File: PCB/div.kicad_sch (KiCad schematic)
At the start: 24 parts

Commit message: :wrench: Adjust project name on sheets
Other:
- title: The Count -> DIV
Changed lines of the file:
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@@
   (paper "A4")
   (title_block
-    (title "The Count")
+    (title "DIV")
     (date "2023-04-03")
     (rev "v1")

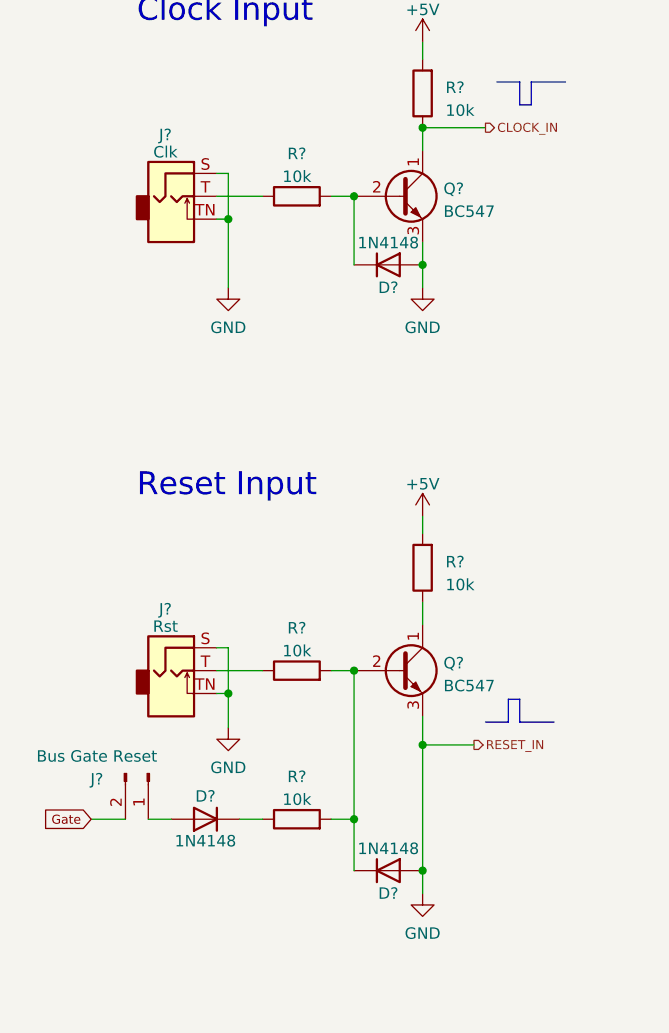
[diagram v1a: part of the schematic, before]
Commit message: :bug: Fix reset input circuit
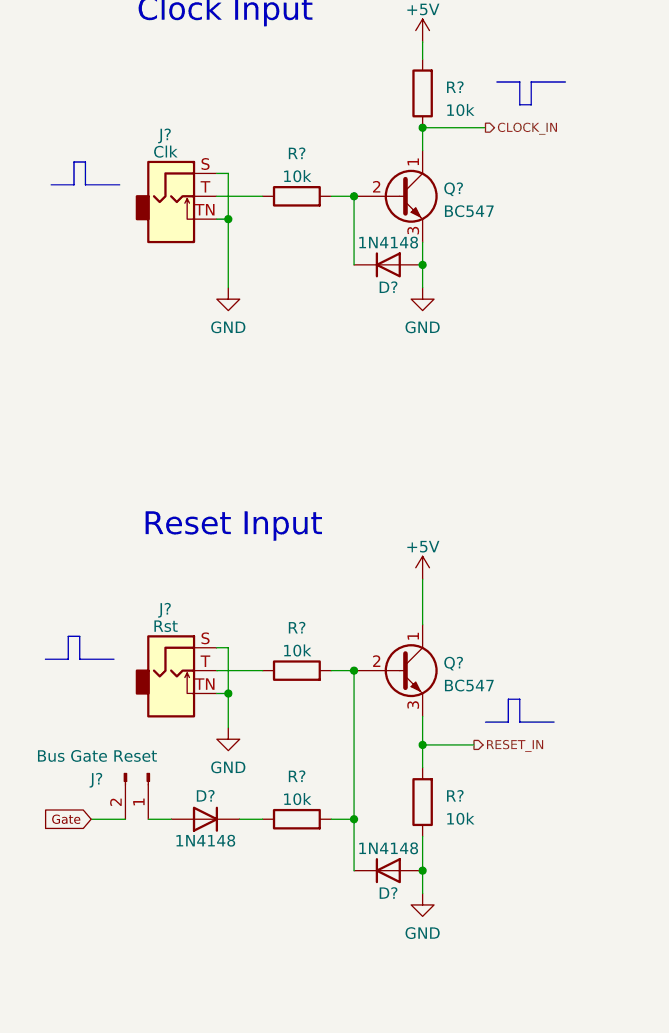
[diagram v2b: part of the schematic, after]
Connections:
- net +5V: now also Q?.1 (C); no longer R?.2
- net GND: now also R?.1; no longer D?.2 (A), Q?.3 (E), U?.2 (MR)
- new net RESET_IN: D?.2 (A), Q?.3 (E), R?.2, U?.2 (MR)
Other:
- moved on the sheet: R?
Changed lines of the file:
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@@
     (stroke (width 0) (type default))
+  )
+  (polyline (pts (xy 21.59 42.545) (xy 21.59 45.085))
+    (stroke (width 0) (type solid))
   )
   (polyline (pts (xy 68.58 104.775) (xy 68.58 102.235))
@@
     (stroke (width 0) (type default))
   )
+  (polyline (pts (xy 20.955 95.25) (xy 20.955 97.79))
+    (stroke (width 0) (type solid))
+  )
   (wire (pts (xy 169.545 74.93) (xy 169.545 78.74))
     (stroke (width 0) (type default))
@@
     (stroke (width 0) (type default))
   )
+  (polyline (pts (xy 19.685 95.25) (xy 20.955 95.25))
+    (stroke (width 0) (type solid))
+  )
   (wire (pts (xy 59.055 121.285) (xy 59.055 123.825))
     (stroke (width 0) (type default))
@@
     (stroke (width 0) (type default))
   )
-  (wire (pts (xy 59.055 81.915) (xy 59.055 83.82))
-    (stroke (width 0) (type default))
-  )
   (wire (pts (xy 36.195 101.6) (xy 37.465 101.6))
     (stroke (width 0) (type default))
@@
     (stroke (width 0) (type default))
   )
-  (wire (pts (xy 59.055 107.315) (xy 59.055 121.285))
+  (wire (pts (xy 59.055 107.315) (xy 59.055 109.855))
     (stroke (width 0) (type default))
   )
@@
     (stroke (width 0) (type default))
   )
+  (polyline (pts (xy 21.59 45.085) (xy 25.4 45.085))
+    (stroke (width 0) (type solid))
+  )
   (wire (pts (xy 46.99 184.15) (xy 46.99 186.69))
     (stroke (width 0) (type default))
@@
     (stroke (width 0) (type default))
   )
+  (polyline (pts (xy 20.32 45.085) (xy 20.32 42.545))
+    (stroke (width 0) (type solid))
+  )
+  (polyline (pts (xy 20.955 97.79) (xy 24.765 97.79))
+    (stroke (width 0) (type solid))
+  )
   (wire (pts (xy 91.44 184.15) (xy 109.22 184.15))
     (stroke (width 0) (type default))
@@
     (stroke (width 0) (type default))
   )
+  (polyline (pts (xy 17.78 45.085) (xy 20.32 45.085))
+    (stroke (width 0) (type solid))
+  )
   (wire (pts (xy 103.505 48.26) (xy 103.505 51.435))
     (stroke (width 0) (type default))
@@
     (stroke (width 0) (type default))
   )
+  (polyline (pts (xy 17.145 97.79) (xy 19.685 97.79))
+    (stroke (width 0) (type solid))
+  )
   (wire (pts (xy 201.93 98.425) (xy 223.52 98.425))
     (stroke (width 0) (type default))
   )
+  (polyline (pts (xy 20.32 42.545) (xy 21.59 42.545))
+    (stroke (width 0) (type solid))
+  )
   (wire (pts (xy 179.705 85.09) (xy 200.025 85.09))
     (stroke (width 0) (type default))
@@
     (stroke (width 0) (type default))
   )
+  (polyline (pts (xy 19.685 97.79) (xy 19.685 95.25))
+    (stroke (width 0) (type solid))
+  )
   (wire (pts (xy 109.22 173.99) (xy 109.22 176.53))
     (stroke (width 0) (type default))
@@
     (stroke (width 0) (type default))
   )
+  (wire (pts (xy 59.055 117.475) (xy 59.055 121.285))
+    (stroke (width 0) (type default))
+  )
   (wire (pts (xy 37.465 48.895) (xy 37.465 56.515))
     (stroke (width 0) (type default))
@@
     (stroke (width 0) (type default))
   )
-  (wire (pts (xy 59.055 91.44) (xy 59.055 93.98))
+  (wire (pts (xy 59.055 88.9) (xy 59.055 93.98))
     (stroke (width 0) (type default))
   )
@@
     (effects (font (size 1 1)) (justify right bottom))
   )
-  (text "Reset Input" (at 27.305 80.01 0)
+  (text "Reset Input" (at 27.94 84.455 0)
     (effects (font (size 2.54 2.54)) (justify left bottom))
   )
@@
     )
   )
-  (symbol (lib_id "Device:R") (at 59.055 87.63 180) (unit 1)
-    (in_bom yes) (on_board yes) (dnp no) (fields_autoplaced)
-    (property "Reference" "R?" (at 61.595 86.995 0)
+  (symbol (lib_id "Device:R") (at 59.055 113.665 180) (unit 1)
+    (in_bom yes) (on_board yes) (dnp no) (fields_autoplaced)
+    (property "Reference" "R?" (at 61.595 113.03 0)
       (effects (font (size 1.27 1.27)) (justify right))
     )
-    (property "Value" "10k" (at 61.595 89.535 0)
+    (property "Value" "10k" (at 61.595 115.57 0)
       (effects (font (size 1.27 1.27)) (justify right))
     )
-    (property "Footprint" "Resistor_THT:R_Axial_DIN0207_L6.3mm_D2.5mm_P7.62mm_Horizontal" (at 60.833 87.63 90)
-      (effects (font (size 1.27 1.27)) hide)
-    )
-    (property "Datasheet" "~" (at 59.055 87.63 0)
+    (property "Footprint" "Resistor_THT:R_Axial_DIN0207_L6.3mm_D2.5mm_P7.62mm_Horizontal" (at 60.833 113.665 90)
+      (effects (font (size 1.27 1.27)) hide)
+    )
+    (property "Datasheet" "~" (at 59.055 113.665 0)
       (effects (font (size 1.27 1.27)) hide)
     )
@@
     )
   )
-  (symbol (lib_id "power:+5V") (at 59.055 81.915 0) (unit 1)
-    (in_bom yes) (on_board yes) (dnp no) (fields_autoplaced)
-    (property "Reference" "#PWR?" (at 59.055 85.725 0)
-      (effects (font (size 1.27 1.27)) hide)
-    )
-    (property "Value" "+5V" (at 59.055 78.3392 0)
+  (symbol (lib_id "power:+5V") (at 59.055 88.9 0) (unit 1)
+    (in_bom yes) (on_board yes) (dnp no) (fields_autoplaced)
+    (property "Reference" "#PWR?" (at 59.055 92.71 0)
+      (effects (font (size 1.27 1.27)) hide)
+    )
+    (property "Value" "+5V" (at 59.055 85.3242 0)
       (effects (font (size 1.27 1.27)))
     )
-    (property "Footprint" "" (at 59.055 81.915 0)
-      (effects (font (size 1.27 1.27)) hide)
-    )
-    (property "Datasheet" "" (at 59.055 81.915 0)
-      (effects (font (size 1.27 1.27)) hide)
-    )
+    (property "Footprint" "" (at 59.055 88.9 0)
+      (effects (font (size 1.27 1.27)) hide)
+    )
+    (property "Datasheet" "" (at 59.055 88.9 0)
+      (effects (font (size 1.27 1.27)) hide)
+    )

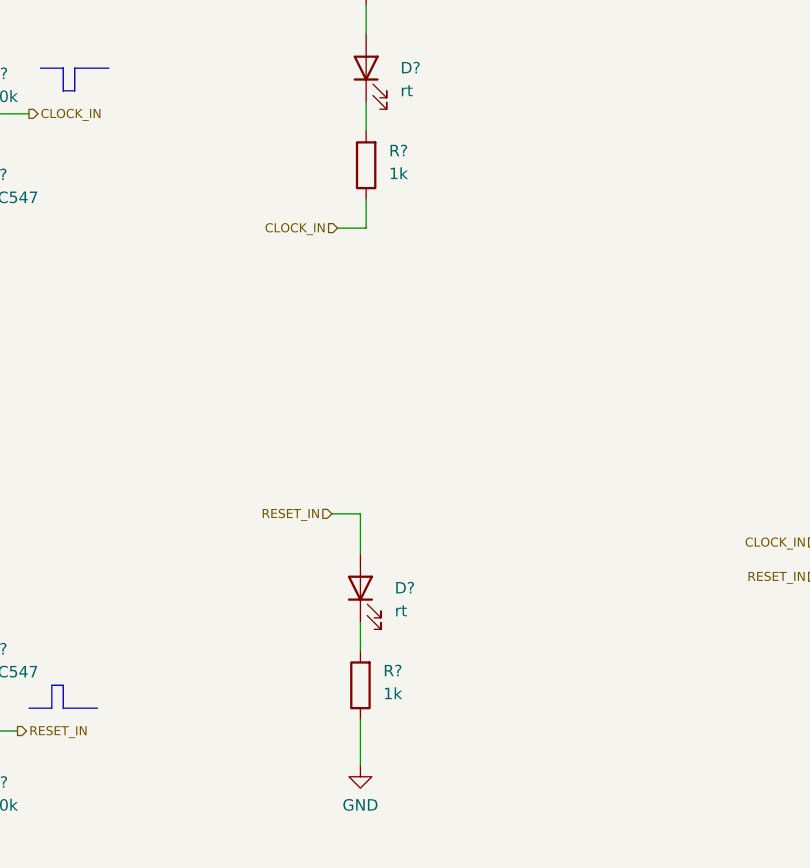
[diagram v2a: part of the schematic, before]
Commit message: :wrench: Adjust LED series resistors
With 4k7 the brightness is much better to look at.
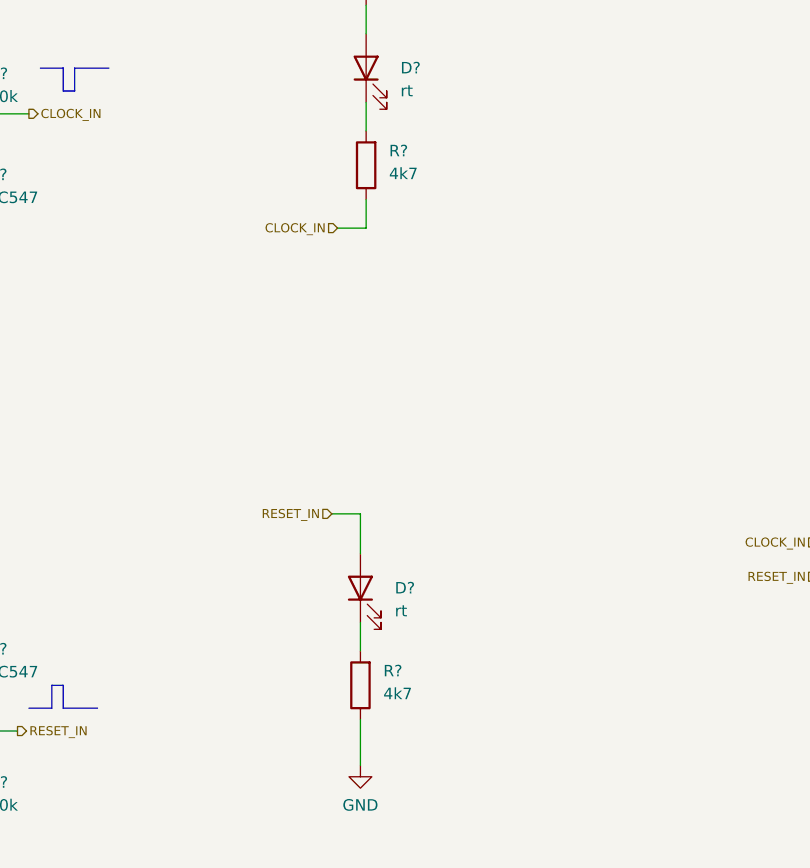
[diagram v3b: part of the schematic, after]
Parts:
- R? (x2): value 1k -> 4k7
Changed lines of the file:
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@@
       (effects (font (size 1.27 1.27)) (justify right))
     )
-    (property "Value" "1k" (at 106.045 45.4025 0)
+    (property "Value" "4k7" (at 106.045 45.4025 0)
       (effects (font (size 1.27 1.27)) (justify right))
     )
@@
       (effects (font (size 1.27 1.27)) (justify right))
     )
-    (property "Value" "1k" (at 105.41 103.1875 0)
-      (effects (font (size 1.27 1.27)) (justify right))
-    )
+    (property "Value" "4k7" (at 105.41 103.1875 0)
+      (effects (font (size 1.27 1.27)) (justify right))
+    )

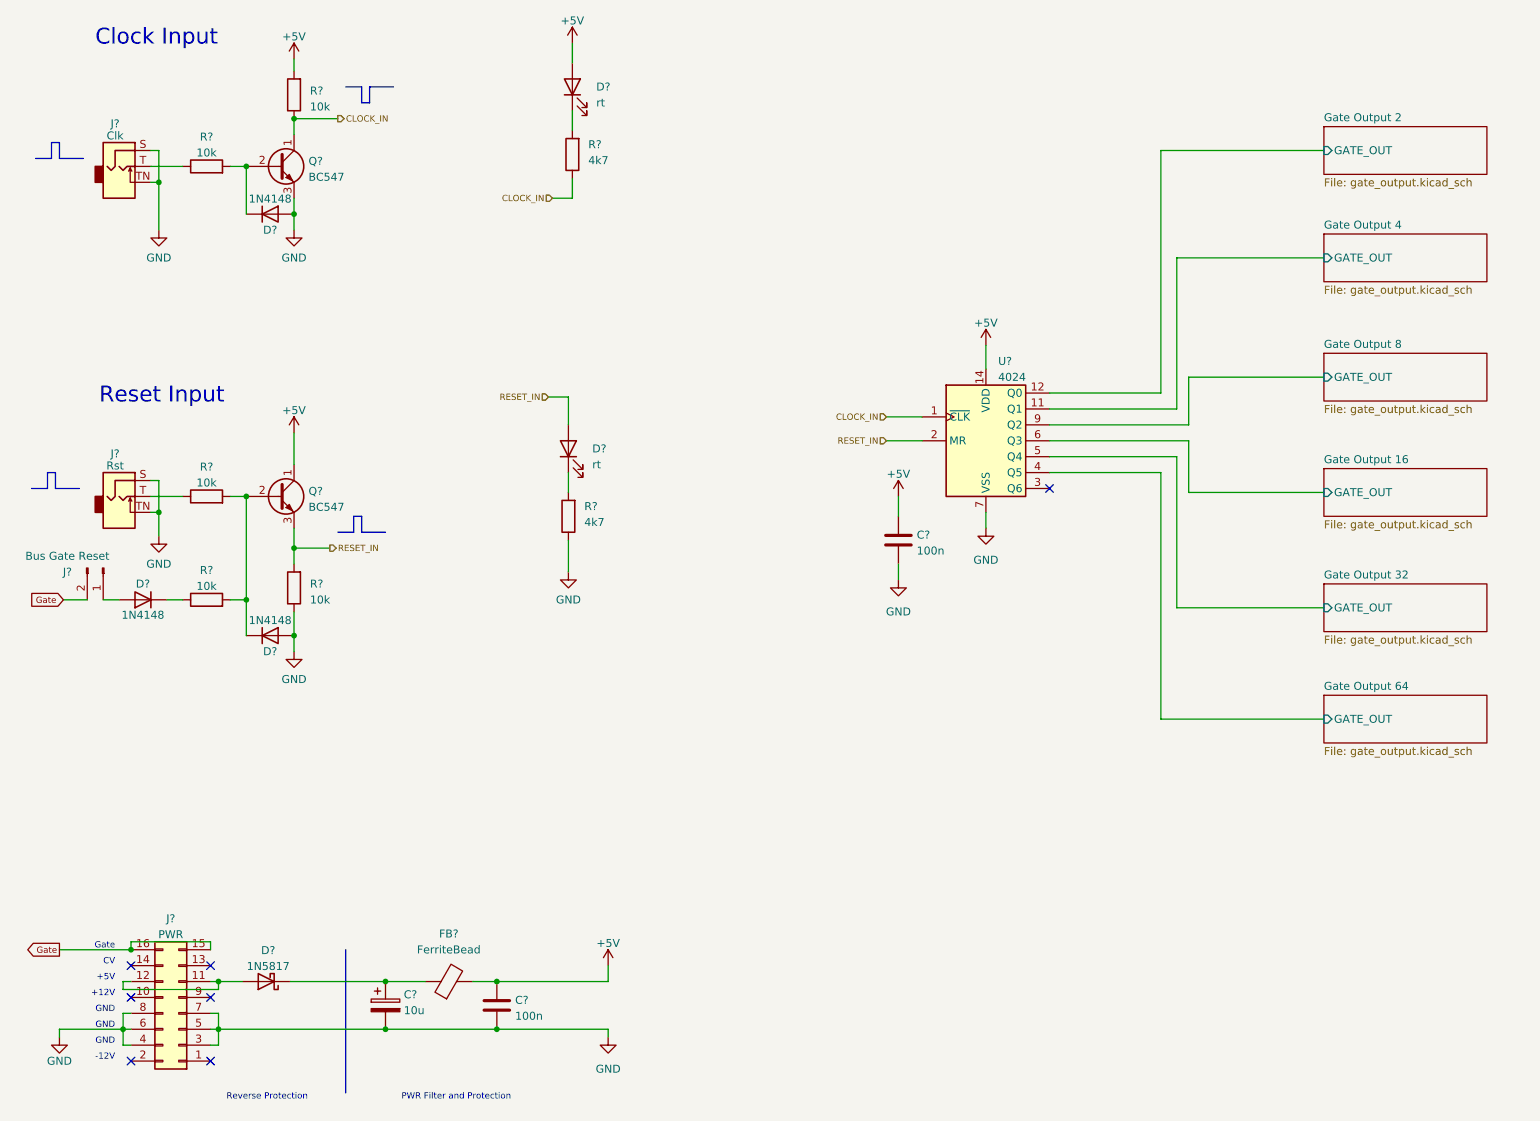
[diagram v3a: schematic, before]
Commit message: :hammer: Switch circuit to 12V supply
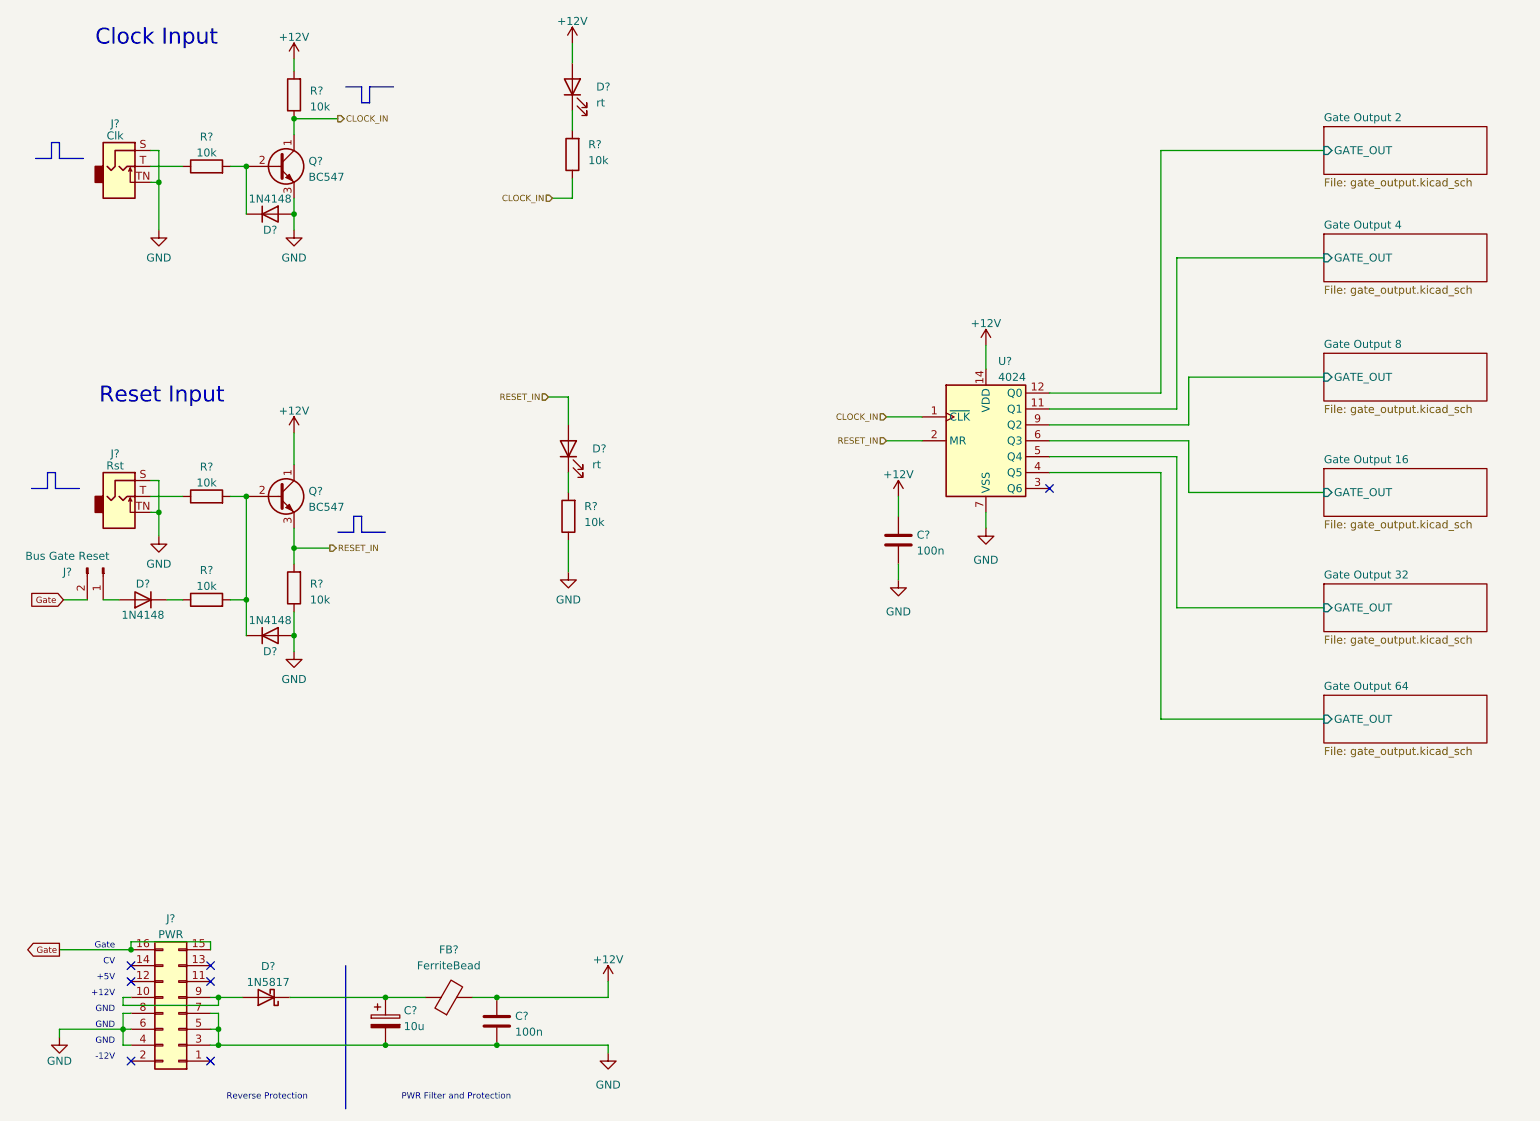
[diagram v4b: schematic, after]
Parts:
- R? (x2): value 4k7 -> 10k
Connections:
- net at J?.10 (Pin_10): now also D?.2 (A), J?.9 (Pin_9)
- net +5V renamed +12V
- now unconnected: J?.11 (Pin_11), J?.12 (Pin_12)
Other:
- moved on the sheet: C?, D?, FB?

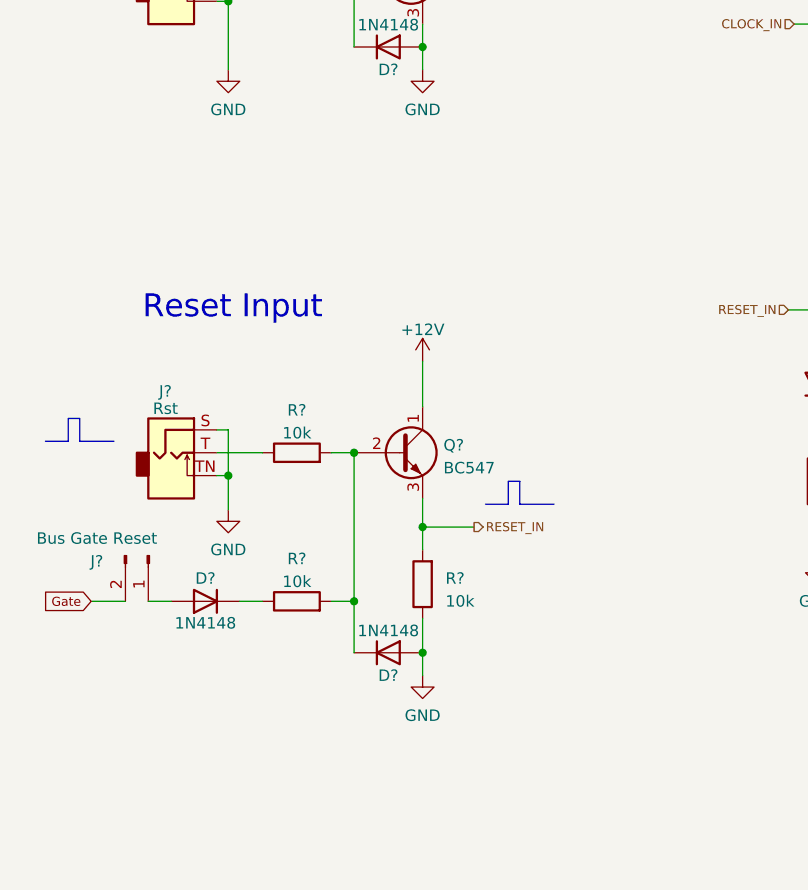
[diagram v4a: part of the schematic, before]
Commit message: :art: Improve reset input to drive 12V
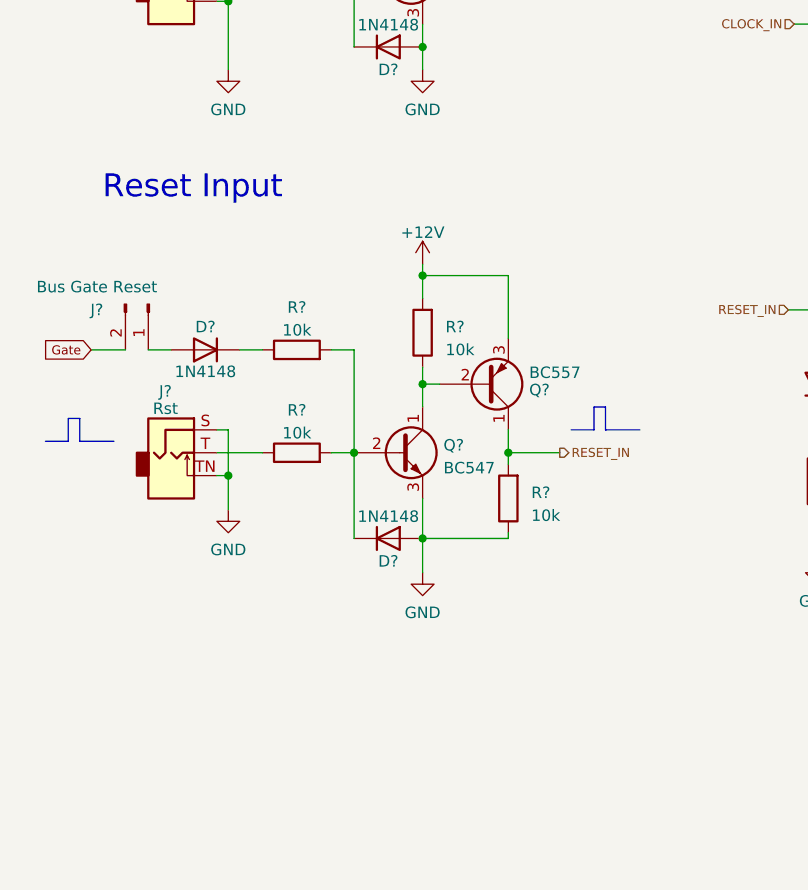
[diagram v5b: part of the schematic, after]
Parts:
- added Q?: BC557, Package_TO_SOT_THT:TO-92_Inline, symbol Transistor_BJT:BC557
- added R?: 10k, Resistor_THT:R_Axial_DIN0207_L6.3mm_D2.5mm_P7.62mm_Horizontal, symbol Device:R
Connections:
- net +12V: now also R?.2, Q?.3 (E); no longer Q?.1 (C)
- net GND: now also Q?.3 (E), R?.1; no longer R?.1
- net RESET_IN: now also Q?.1 (C), R?.2; no longer Q?.3 (E), R?.2
- new net: Q?.1 (C), Q?.2 (B), R?.1
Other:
- moved on the sheet: D?, J?, R?
